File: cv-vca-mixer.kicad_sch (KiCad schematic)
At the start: 46 parts, among them Q901 Q_PNP_BEC, Q902 Q_PNP_BEC, U901 MCP6004, U902 MCP6004, U903 LM13700

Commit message: CV VCA / Mixer wip
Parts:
- renumbered U902 to U901, U901 to U902
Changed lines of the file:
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@@
   (symbol (lib_id "Amplifier_Operational:MCP6004") (at 219.71 157.48 0) (mirror x) (unit 4)
     (in_bom yes) (on_board yes) (fields_autoplaced)
-    (property "Reference" "U901" (id 0) (at 219.71 147.32 0))
+    (property "Reference" "U902" (id 0) (at 219.71 147.32 0))
     (property "Value" "MCP6004" (id 1) (at 219.71 149.86 0))
     (property "Footprint" "Package_SO:SOIC-14_3.9x8.7mm_P1.27mm" (id 2) (at 218.44 160.02 0)
@@
   (symbol (lib_id "Amplifier_Operational:MCP6004") (at 247.65 50.8 0) (mirror x) (unit 4)
     (in_bom yes) (on_board yes) (fields_autoplaced)
-    (property "Reference" "U902" (id 0) (at 247.65 40.64 0))
+    (property "Reference" "U901" (id 0) (at 247.65 40.64 0))
     (property "Value" "MCP6004" (id 1) (at 247.65 43.18 0))
     (property "Footprint" "Package_SO:SOIC-14_3.9x8.7mm_P1.27mm" (id 2) (at 246.38 53.34 0)

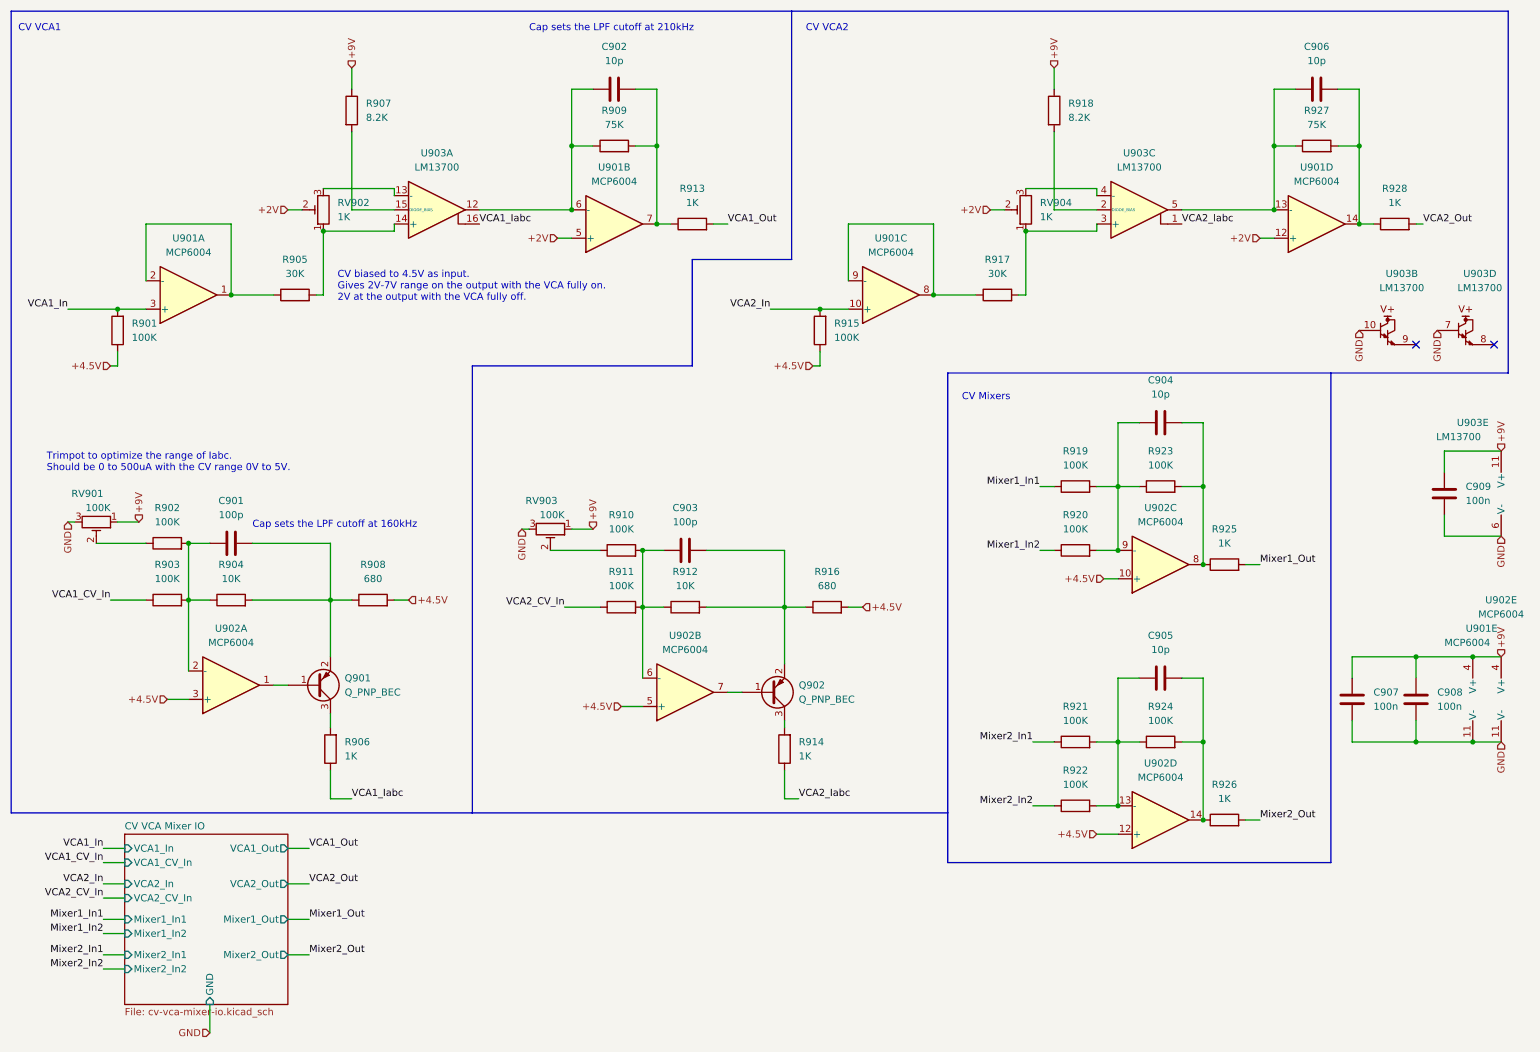
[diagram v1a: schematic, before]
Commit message: CV VCA Mixer & audio VCA layout done
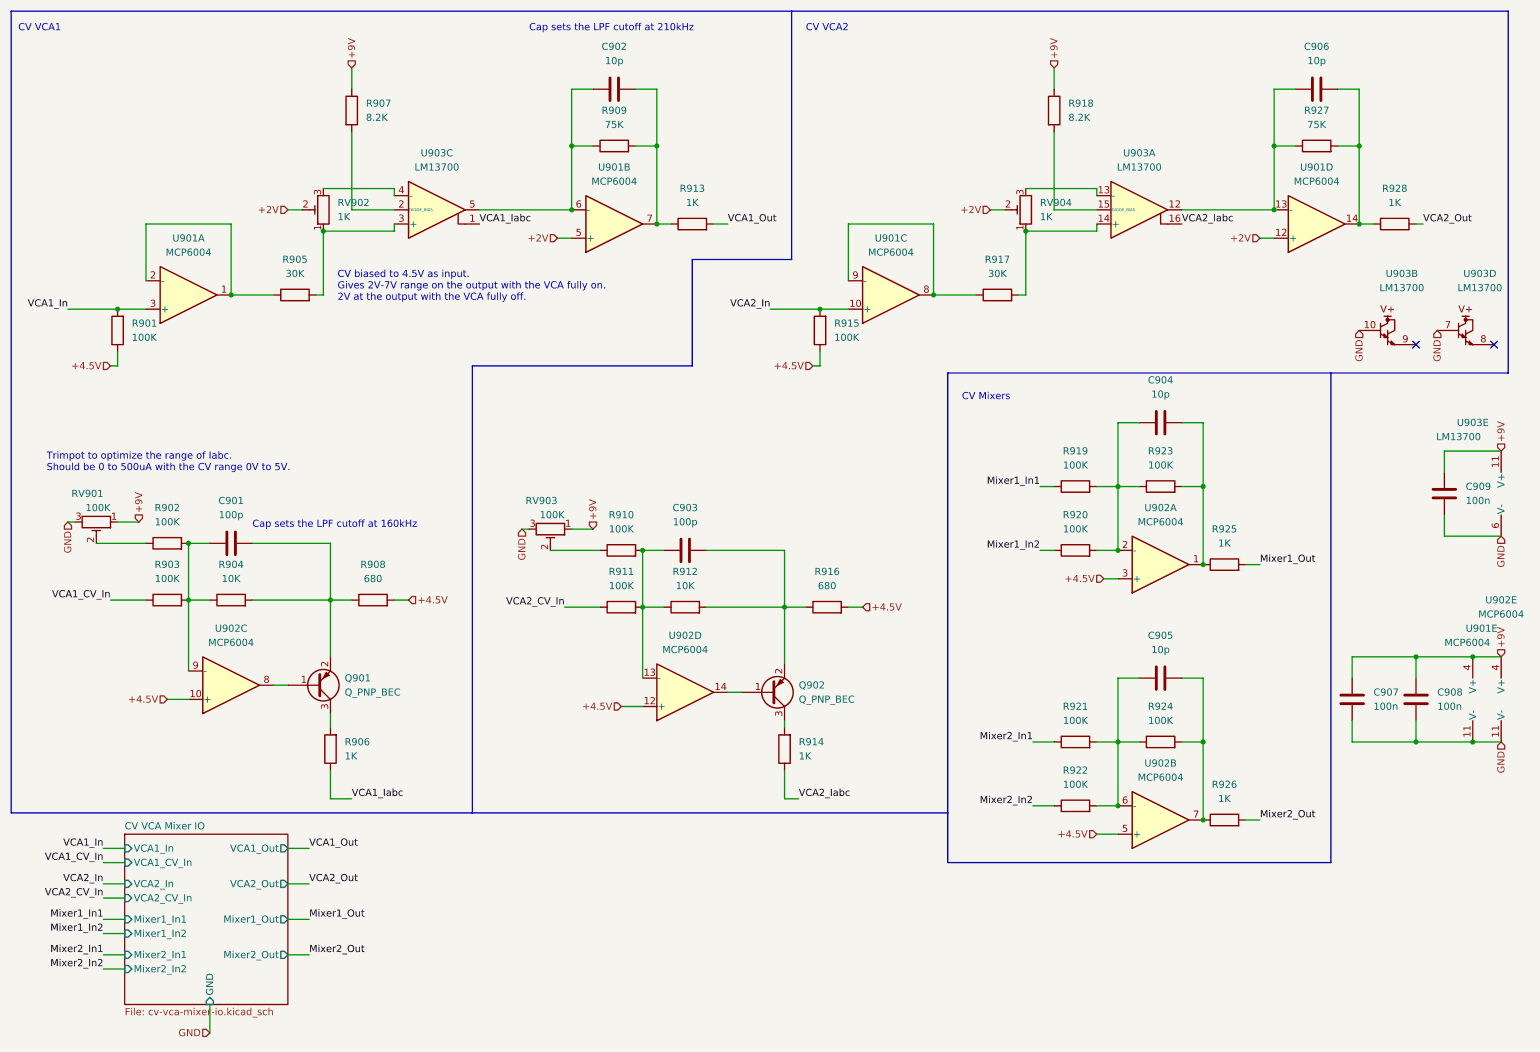
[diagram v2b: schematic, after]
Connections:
- net +4.5V: now also U902.10 (+), U902.12 (+), U902.3 (+), U902.5 (+); no longer U902.10 (+), U902.12 (+), U902.3 (+), U902.5 (+)
- net VCA1_Iabc: now also U903.1; no longer U903.16
- net VCA2_Iabc: now also U903.16; no longer U903.1
- net at R905.2, RV902.1: now also U903.3 (+); no longer U903.14 (+)
- net at C903.1, R910.2, R911.2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: now also U902.13 (-); no longer U902.6 (-)
- net at C906.2, R927.1, U901.13 (-): now also U903.12; no longer U903.5
- net at R917.2, RV904.1: now also U903.14 (+); no longer U903.3 (+)
- net at R918.2: now also U903.15 (DIODE_BIAS); no longer U903.2 (DIODE_BIAS)
- net at RV904.3: now also U903.13 (-); no longer U903.4 (-)
- net at C904.1, R919.2, R920.2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: now also U902.2 (-); no longer U902.9 (-)
- net at C904.2, R923.2, R925.1: now also U902.1; no longer U902.8
- net at C905.1, R921.2, R922.2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: now also U902.6 (-); no longer U902.13 (-)
- net at C905.2, R924.2, R926.1: now also U902.7; no longer U902.14
- net at RV902.3: now also U903.4 (-); no longer U903.13 (-)
- net at R907.2: now also U903.2 (DIODE_BIAS); no longer U903.15 (DIODE_BIAS)
- net at C901.1, R902.2, R903.2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: now also U902.9 (-); no longer U902.2 (-)
- net at Q902.1 (B): now also U902.14; no longer U902.7
- net at C902.2, R909.1, U901.6 (-): now also U903.5; no longer U903.12
- net at Q901.1 (B): now also U902.8; no longer U902.1
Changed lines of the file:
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@@
     (pin "6")
   )
-  (symbol (lib_id "Amplifier_Operational:LM13700") (at 215.9 48.26 0) (unit 3)
+  (symbol (lib_id "Amplifier_Operational:LM13700") (at 215.9 48.26 0) (unit 1)
     (in_bom yes) (on_board yes) (fields_autoplaced)
     (property "Reference" "U903" (id 0) (at 215.9 38.1 0))
@@
     (pin "2")
   )
-  (symbol (lib_id "Amplifier_Operational:MCP6004") (at 219.71 157.48 0) (mirror x) (unit 4)
+  (symbol (lib_id "Amplifier_Operational:MCP6004") (at 219.71 157.48 0) (mirror x) (unit 2)
     (in_bom yes) (on_board yes) (fields_autoplaced)
     (property "Reference" "U902" (id 0) (at 219.71 147.32 0))
@@
     (pin "2")
   )
-  (symbol (lib_id "Amplifier_Operational:MCP6004") (at 134.62 134.62 0) (mirror x) (unit 2)
+  (symbol (lib_id "Amplifier_Operational:MCP6004") (at 134.62 134.62 0) (mirror x) (unit 4)
     (in_bom yes) (on_board yes) (fields_autoplaced)
     (property "Reference" "U902" (id 0) (at 134.62 124.46 0))
@@
     (pin "2")
   )
-  (symbol (lib_id "Amplifier_Operational:LM13700") (at 90.17 48.26 0) (unit 1)
+  (symbol (lib_id "Amplifier_Operational:LM13700") (at 90.17 48.26 0) (unit 3)
     (in_bom yes) (on_board yes) (fields_autoplaced)
     (property "Reference" "U903" (id 0) (at 90.17 38.1 0))
@@
     (pin "2")
   )
-  (symbol (lib_id "Amplifier_Operational:MCP6004") (at 53.34 133.35 0) (mirror x) (unit 1)
+  (symbol (lib_id "Amplifier_Operational:MCP6004") (at 53.34 133.35 0) (mirror x) (unit 3)
     (in_bom yes) (on_board yes) (fields_autoplaced)
     (property "Reference" "U902" (id 0) (at 53.34 123.19 0))
@@
     (pin "2")
   )
-  (symbol (lib_id "Amplifier_Operational:MCP6004") (at 219.71 111.76 0) (mirror x) (unit 3)
+  (symbol (lib_id "Amplifier_Operational:MCP6004") (at 219.71 111.76 0) (mirror x) (unit 1)
     (in_bom yes) (on_board yes) (fields_autoplaced)
     (property "Reference" "U902" (id 0) (at 219.71 101.6 0))
